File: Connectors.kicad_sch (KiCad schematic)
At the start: 1 part, among them J10 Conn_01x30_Pin

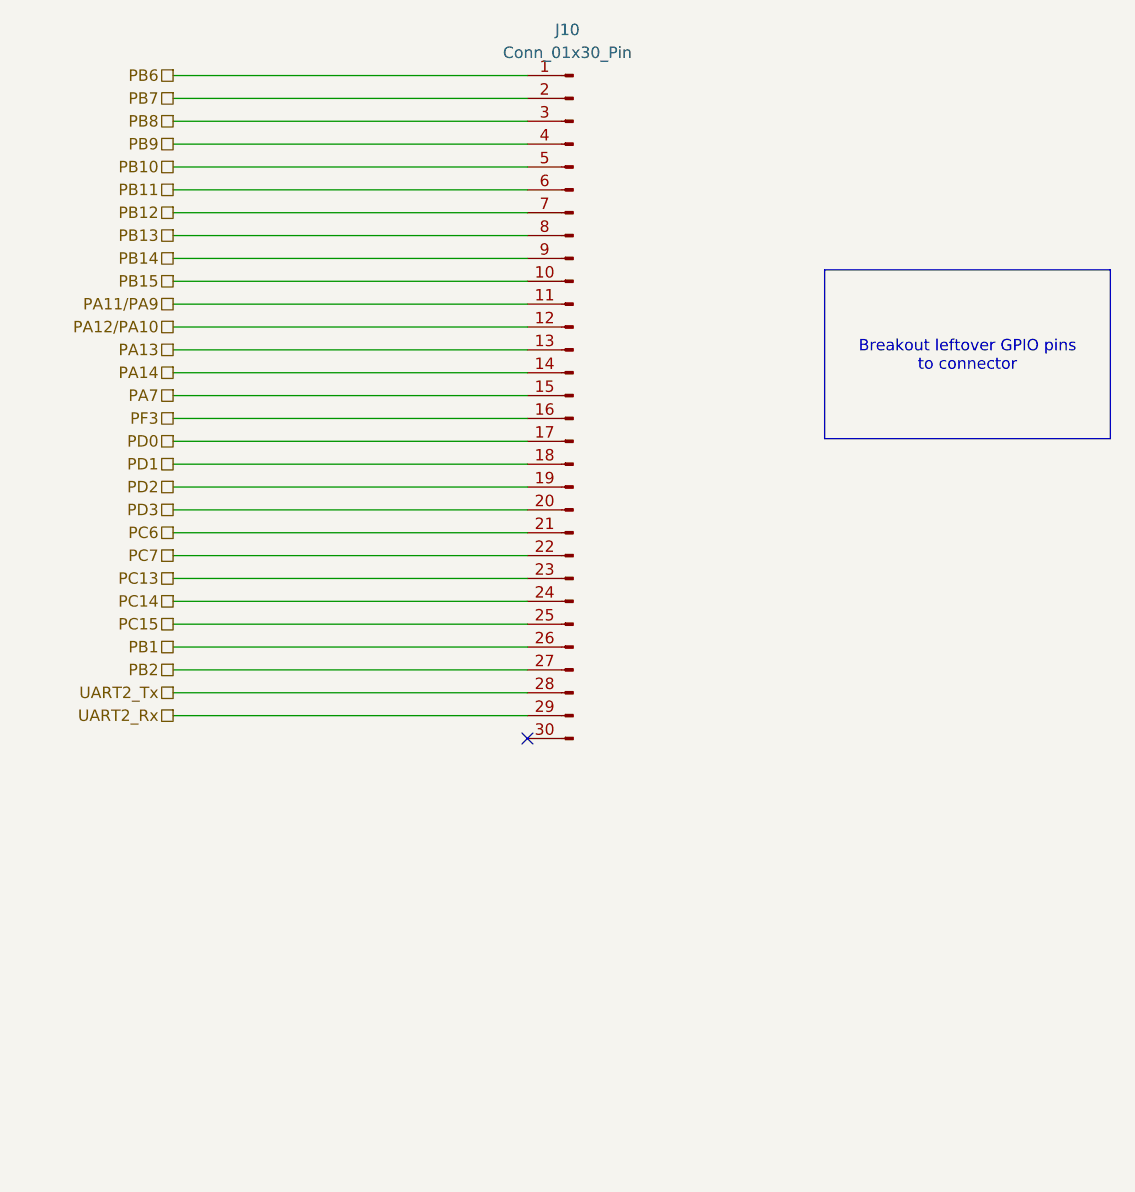
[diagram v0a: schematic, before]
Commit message: changed schematics
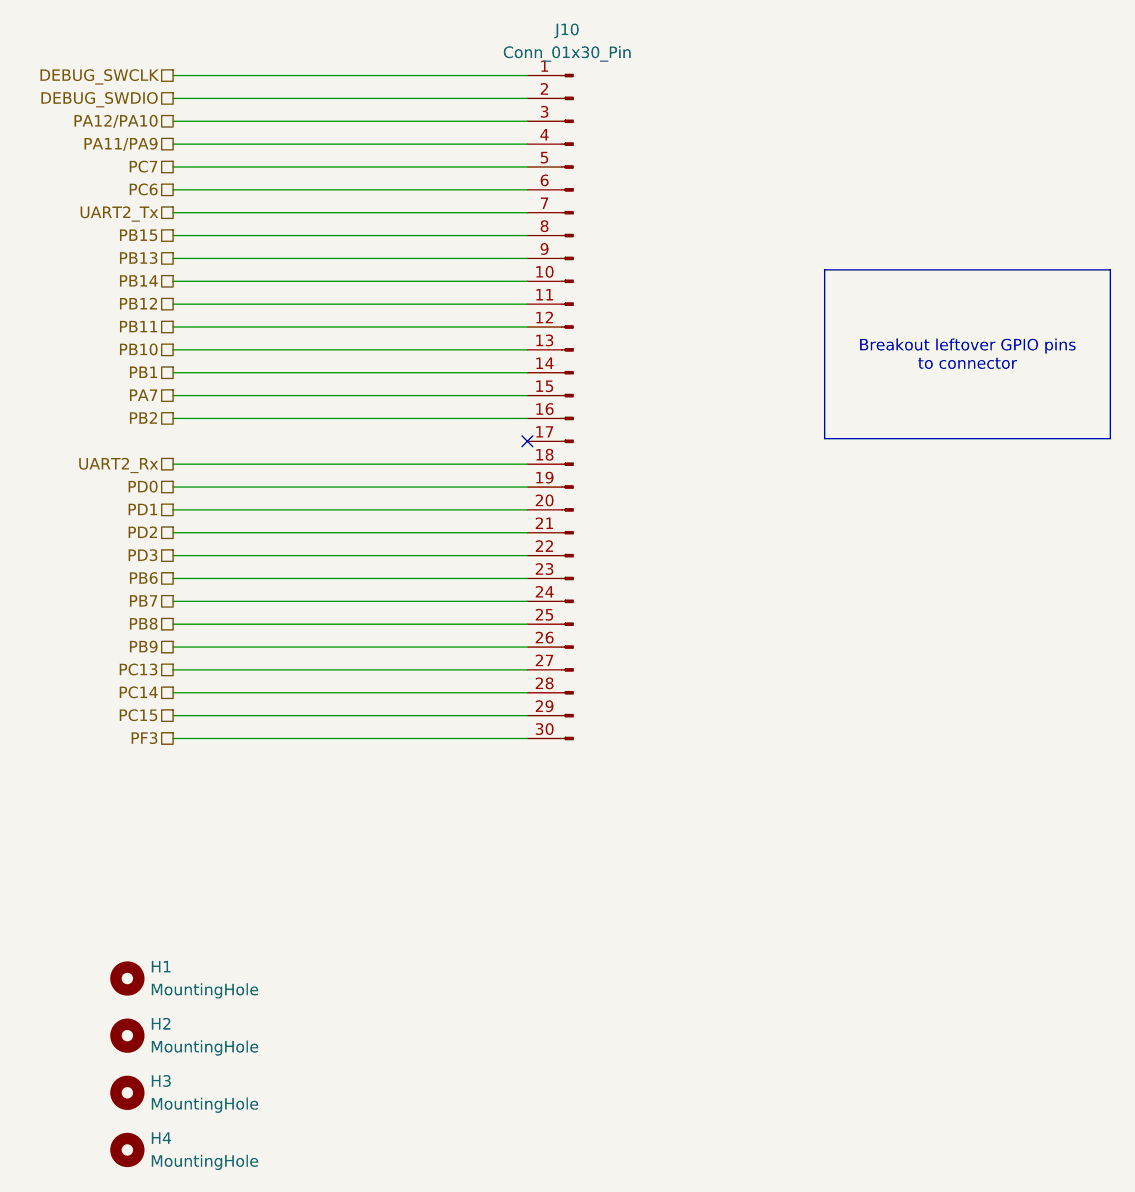
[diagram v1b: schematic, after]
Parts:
- added H1, H2, H3, H4: MountingHole, MountingHole:MountingHole_3.2mm_M3, symbol Mechanical:MountingHole
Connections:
- net PA13 is gone; now on net PB10: J10.13 (Pin_13)
- net PA14 is gone; now on net PB1: J10.14 (Pin_14)
- net PA11/PA9: now also J10.4 (Pin_4); no longer J10.11 (Pin_11)
- net PA12/PA10: now also J10.3 (Pin_3); no longer J10.12 (Pin_12)
- net PB1: no longer J10.26 (Pin_26)
- net PB10: no longer J10.5 (Pin_5)
- net PB11: now also J10.12 (Pin_12); no longer J10.6 (Pin_6)
- net PB12: now also J10.11 (Pin_11); no longer J10.7 (Pin_7)
- net PB13: now also J10.9 (Pin_9); no longer J10.8 (Pin_8)
- net PB14: now also J10.10 (Pin_10); no longer J10.9 (Pin_9)
- net PB15: now also J10.8 (Pin_8); no longer J10.10 (Pin_10)
- net PB2: now also J10.16 (Pin_16); no longer J10.27 (Pin_27)
- net PB6: now also J10.23 (Pin_23); no longer J10.1 (Pin_1)
- net PB7: now also J10.24 (Pin_24); no longer J10.2 (Pin_2)
- net PB8: now also J10.25 (Pin_25); no longer J10.3 (Pin_3)
- net PB9: now also J10.26 (Pin_26); no longer J10.4 (Pin_4)
- net PC13: now also J10.27 (Pin_27); no longer J10.23 (Pin_23)
- net PC14: now also J10.28 (Pin_28); no longer J10.24 (Pin_24)
- net PC15: now also J10.29 (Pin_29); no longer J10.25 (Pin_25)
- net PC6: now also J10.6 (Pin_6); no longer J10.21 (Pin_21)
- net PC7: now also J10.5 (Pin_5); no longer J10.22 (Pin_22)
- net PD0: now also J10.19 (Pin_19); no longer J10.17 (Pin_17)
- net PD1: now also J10.20 (Pin_20); no longer J10.18 (Pin_18)
- net PD2: now also J10.21 (Pin_21); no longer J10.19 (Pin_19)
- net PD3: now also J10.22 (Pin_22); no longer J10.20 (Pin_20)
- net PF3: now also J10.30 (Pin_30); no longer J10.16 (Pin_16)
- net UART2_Rx: now also J10.18 (Pin_18); no longer J10.29 (Pin_29)
- net UART2_Tx: now also J10.7 (Pin_7); no longer J10.28 (Pin_28)
- new net DEBUG_SWCLK: J10.1 (Pin_1)
- new net DEBUG_SWDIO: J10.2 (Pin_2)
